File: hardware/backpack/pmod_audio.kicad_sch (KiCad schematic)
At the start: 1 part, among them J1 Conn_01x14_Socket

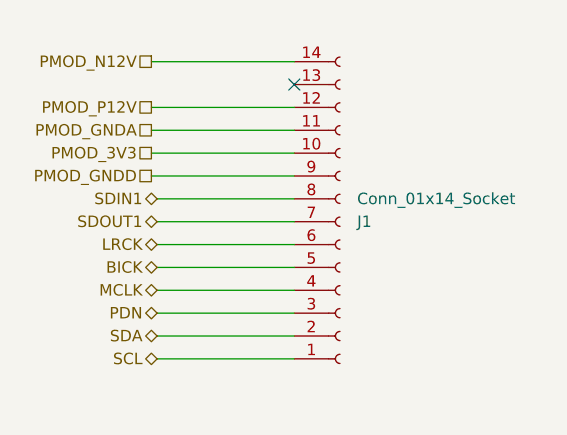
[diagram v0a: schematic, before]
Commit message: fix footprint errors and pin assignments on ffc
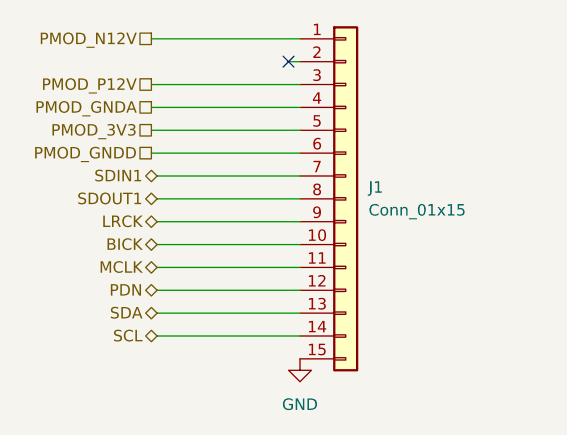
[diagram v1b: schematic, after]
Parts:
- removed J1: Conn_01x14_Socket, ffc-ctxj:FFC_0.5-14P_CTXJ-H2.0_1, symbol Connector:Conn_01x14_Socket
- added J1: Conn_01x15, ffc-ctxj:FFC_0.5-14P_CTXJ-H2.0_1, symbol Connector_Generic:Conn_01x15
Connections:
- net BICK: now also J1.10 (Pin_10)
- net LRCK: now also J1.9 (Pin_9)
- net MCLK: now also J1.11 (Pin_11)
- net PDN: now also J1.12 (Pin_12)
- net PMOD_3V3: now also J1.5 (Pin_5)
- net PMOD_GNDA: now also J1.4 (Pin_4)
- net PMOD_GNDD: now also J1.6 (Pin_6)
- net PMOD_N12V: now also J1.1 (Pin_1)
- net PMOD_P12V: now also J1.3 (Pin_3)
- net SCL: now also J1.14 (Pin_14)
- net SDA: now also J1.13 (Pin_13)
- net SDIN1: now also J1.7 (Pin_7)
- net SDOUT1: now also J1.8 (Pin_8)
- new net GND: J1.15 (Pin_15)
